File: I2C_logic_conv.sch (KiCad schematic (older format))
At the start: 5 parts

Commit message: アートワーク開始
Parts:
- Q1: renamed from Q?; footprint (none) -> SMD_Packages:SOT363
- R24, R25, R26, R27: renamed from R?; footprint (none) -> Resistors_SMD:R_0603
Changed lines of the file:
@@
 $Descr A4 11693 8268
 encoding utf-8
-Sheet 3 4
+Sheet 2 5
 Title ""
 Date ""
@@
 $EndDescr
 $Comp
-L BSS138PS Q?
+L BSS138PS Q1
 U 1 1 5838B8C7
 P 5850 3450
-AR Path="/583898DE/5838B8C7" Ref="Q?"  Part="1"
-AR Path="/58389DA7/5838B8C7" Ref="Q?"  Part="1"
-F 0 "Q?" H 6050 3900 50  0000 L CNN
+AR Path="/58389DA7/5838B8C7" Ref="Q1"  Part="1"
+AR Path="/583898DE/5838B8C7" Ref="Q2"  Part="1"
+AR Path="/583E5F3D/5838B8C7" Ref="Q3"  Part="1"
+F 0 "Q3" H 6050 3900 50  0000 L CNN
 F 1 "BSS138PS" H 5600 3900 50  0000 L CNN
-F 2 "" V 5775 3850 50  0001 L CIN
+F 2 "SMD_Packages:SOT363" V 5775 3850 50  0001 L CIN
 F 3 "" V 5850 3650 50  0000 L CNN
 	1    5850 3450
@@
 	5600 3550 4850 3550
 $Comp
-L R R?
+L R R24
 U 1 1 5838B993
 P 5050 2950
-AR Path="/583898DE/5838B993" Ref="R?"  Part="1"
-AR Path="/58389DA7/5838B993" Ref="R?"  Part="1"
-F 0 "R?" V 5130 2950 50  0000 C CNN
+AR Path="/58389DA7/5838B993" Ref="R24"  Part="1"
+AR Path="/583898DE/5838B993" Ref="R28"  Part="1"
+AR Path="/583E5F3D/5838B993" Ref="R33"  Part="1"
+F 0 "R33" V 5130 2950 50  0000 C CNN
 F 1 "R" V 5050 2950 50  0000 C CNN
-F 2 "" V 4980 2950 50  0000 C CNN
+F 2 "Resistors_SMD:R_0603" V 4980 2950 50  0001 C CNN
 F 3 "" H 5050 2950 50  0000 C CNN
 	1    5050 2950
@@
 $EndComp
 $Comp
-L R R?
+L R R25
 U 1 1 5838BA42
 P 5250 2950
-AR Path="/583898DE/5838BA42" Ref="R?"  Part="1"
-AR Path="/58389DA7/5838BA42" Ref="R?"  Part="1"
-F 0 "R?" V 5330 2950 50  0000 C CNN
+AR Path="/58389DA7/5838BA42" Ref="R25"  Part="1"
+AR Path="/583898DE/5838BA42" Ref="R29"  Part="1"
+AR Path="/583E5F3D/5838BA42" Ref="R34"  Part="1"
+F 0 "R34" V 5330 2950 50  0000 C CNN
 F 1 "R" V 5250 2950 50  0000 C CNN
-F 2 "" V 5180 2950 50  0000 C CNN
+F 2 "Resistors_SMD:R_0603" V 5180 2950 50  0001 C CNN
 F 3 "" H 5250 2950 50  0000 C CNN
 	1    5250 2950
@@
 Connection ~ 5250 3550
 $Comp
-L R R?
+L R R26
 U 1 1 5838BBE6
 P 6300 2900
-AR Path="/583898DE/5838BBE6" Ref="R?"  Part="1"
-AR Path="/58389DA7/5838BBE6" Ref="R?"  Part="1"
-F 0 "R?" V 6380 2900 50  0000 C CNN
+AR Path="/58389DA7/5838BBE6" Ref="R26"  Part="1"
+AR Path="/583898DE/5838BBE6" Ref="R30"  Part="1"
+AR Path="/583E5F3D/5838BBE6" Ref="R35"  Part="1"
+F 0 "R35" V 6380 2900 50  0000 C CNN
 F 1 "R" V 6300 2900 50  0000 C CNN
-F 2 "" V 6230 2900 50  0000 C CNN
+F 2 "Resistors_SMD:R_0603" V 6230 2900 50  0001 C CNN
 F 3 "" H 6300 2900 50  0000 C CNN
 	1    6300 2900
@@
 $EndComp
 $Comp
-L R R?
+L R R27
 U 1 1 5838BC03
 P 6500 2900
-AR Path="/583898DE/5838BC03" Ref="R?"  Part="1"
-AR Path="/58389DA7/5838BC03" Ref="R?"  Part="1"
-F 0 "R?" V 6580 2900 50  0000 C CNN
+AR Path="/58389DA7/5838BC03" Ref="R27"  Part="1"
+AR Path="/583898DE/5838BC03" Ref="R31"  Part="1"
+AR Path="/583E5F3D/5838BC03" Ref="R36"  Part="1"
+F 0 "R36" V 6580 2900 50  0000 C CNN
 F 1 "R" V 6500 2900 50  0000 C CNN
-F 2 "" V 6430 2900 50  0000 C CNN
+F 2 "Resistors_SMD:R_0603" V 6430 2900 50  0001 C CNN
 F 3 "" H 6500 2900 50  0000 C CNN
 	1    6500 2900

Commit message: 進捗
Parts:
- removed Q1: BSS138PS, SMD_Packages:SOT363, symbol BSS138PS
- added C6, C7: C, Capacitors_SMD:C_0603, symbol C
- added R14: R, Resistors_SMD:R_0603, symbol R
- added U4: PCA9306, Housings_SSOP:MSOP-8_3x3mm_Pitch0.65mm, symbol PCA9306
- renumbered R24 to R12, R25 to R13, R26 to R15, R27 to R16
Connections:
- net HV1: now also U4.6 (SCL2)
- net HV2: now also U4.5 (SDA2)
- net LV1: now also U4.3 (SCL1)
- net LV2: now also U4.4 (SDA1)
- net VH: now also R14.1
- net VL: now also C6.2, U4.2 (VREF1)
- new net: C7.2, R14.2, U4.7 (VREF2), U4.8 (EN)
- new net GND: C6.1, C7.1, U4.1 (GND)
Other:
- moved on the sheet: R23, R24, R26, R27

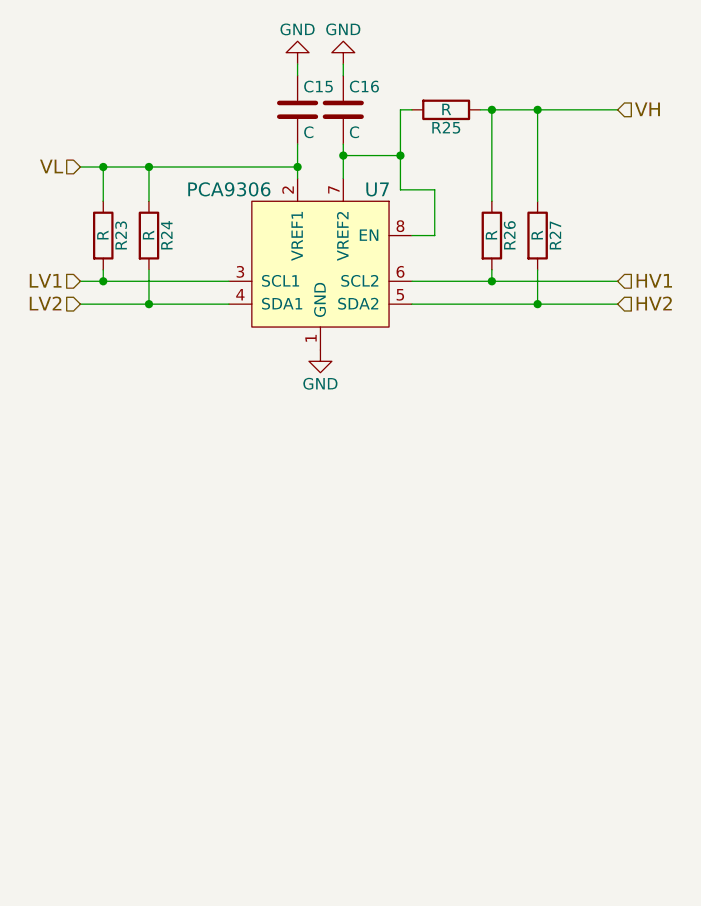
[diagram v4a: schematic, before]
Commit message: 図面にタイトルを追加
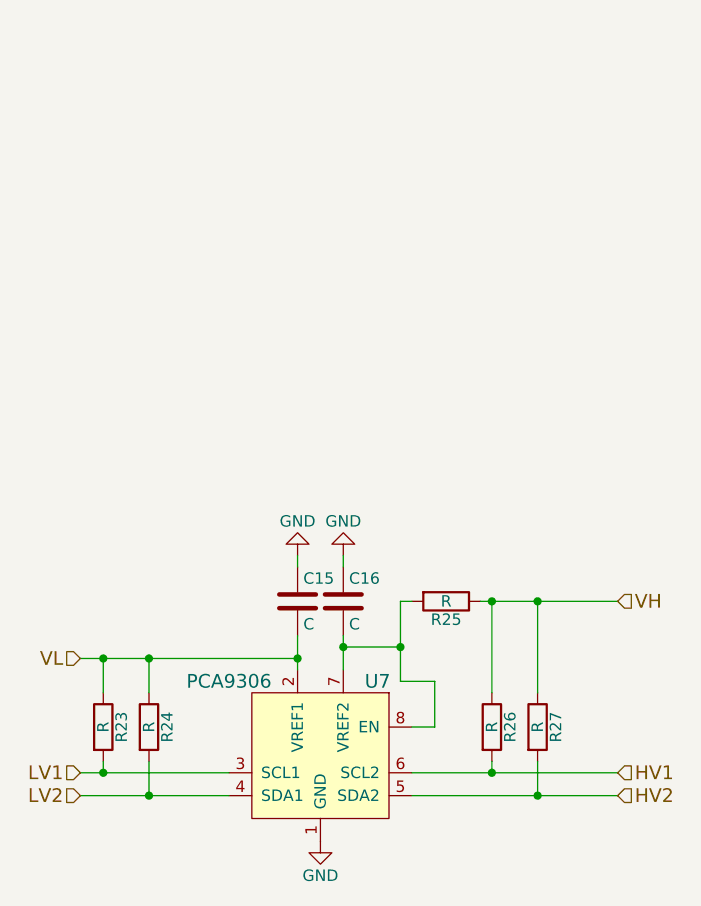
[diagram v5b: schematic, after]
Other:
- moved on the sheet: C15, C16, R23, R24, R25, R26, R27, U7
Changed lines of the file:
@@
 encoding utf-8
 Sheet 5 5
-Title ""
-Date ""
-Rev ""
-Comp ""
-Comment1 ""
-Comment2 ""
+Title "JetsonTK1_GPIO_Connector"
+Date "2016-12-18"
+Rev "1.1"
+Comp "Manju-Honpo"
+Comment1 "@C91"
+Comment2 "Designed by @yuqlid"
 Comment3 ""
 Comment4 ""
 $EndDescr
 Wire Wire Line
-	6300 2200 7200 2200
-Wire Wire Line
-	6300 2300 7200 2300
-Wire Wire Line
-	4850 2200 5500 2200
-Wire Wire Line
-	4850 2300 5500 2300
+	6300 4350 7200 4350
+Wire Wire Line
+	6300 4450 7200 4450
+Wire Wire Line
+	4850 4350 5500 4350
+Wire Wire Line
+	4850 4450 5500 4450
 $Comp
 L R R12
 U 1 1 5838B993
-P 4950 2000
+P 4950 4150
 AR Path="/58389DA7/5838B993" Ref="R12"  Part="1"
 AR Path="/583898DE/5838B993" Ref="R17"  Part="1"
 AR Path="/583E5F3D/5838B993" Ref="R23"  Part="1"
-F 0 "R23" V 5030 2000 50  0000 C CNN
-F 1 "R" V 4950 2000 50  0000 C CNN
-F 2 "Resistors_SMD:R_0603" V 4880 2000 50  0001 C CNN
-F 3 "" H 4950 2000 50  0000 C CNN
-	1    4950 2000
+F 0 "R23" V 5030 4150 50  0000 C CNN
+F 1 "R" V 4950 4150 50  0000 C CNN
+F 2 "Resistors_SMD:R_0603" V 4880 4150 50  0001 C CNN
+F 3 "" H 4950 4150 50  0000 C CNN
+	1    4950 4150
 	1    0    0    -1
 $EndComp
@@
 L R R13
 U 1 1 5838BA42
-P 5150 2000
+P 5150 4150
 AR Path="/58389DA7/5838BA42" Ref="R13"  Part="1"
 AR Path="/583898DE/5838BA42" Ref="R18"  Part="1"
 AR Path="/583E5F3D/5838BA42" Ref="R24"  Part="1"
-F 0 "R24" V 5230 2000 50  0000 C CNN
-F 1 "R" V 5150 2000 50  0000 C CNN
-F 2 "Resistors_SMD:R_0603" V 5080 2000 50  0001 C CNN
-F 3 "" H 5150 2000 50  0000 C CNN
-	1    5150 2000
-	1    0    0    -1
-$EndComp
-Wire Wire Line
-	4850 1700 5800 1700
-Wire Wire Line
-	5150 1850 5150 1700
-Connection ~ 5150 1700
-Wire Wire Line
-	4950 1850 4950 1700
-Connection ~ 4950 1700
-Wire Wire Line
-	4950 2150 4950 2200
-Connection ~ 4950 2200
-Wire Wire Line
-	5150 2150 5150 2300
-Connection ~ 5150 2300
+F 0 "R24" V 5230 4150 50  0000 C CNN
+F 1 "R" V 5150 4150 50  0000 C CNN
+F 2 "Resistors_SMD:R_0603" V 5080 4150 50  0001 C CNN
+F 3 "" H 5150 4150 50  0000 C CNN
+	1    5150 4150
+	1    0    0    -1
+$EndComp
+Wire Wire Line
+	4850 3850 5800 3850
+Wire Wire Line
+	5150 4000 5150 3850
+Connection ~ 5150 3850
+Wire Wire Line
+	4950 4000 4950 3850
+Connection ~ 4950 3850
+Wire Wire Line
+	4950 4300 4950 4350
+Connection ~ 4950 4350
+Wire Wire Line
+	5150 4300 5150 4450
+Connection ~ 5150 4450
 $Comp
 L R R15
 U 1 1 5838BBE6
-P 6650 2000
+P 6650 4150
 AR Path="/58389DA7/5838BBE6" Ref="R15"  Part="1"
 AR Path="/583898DE/5838BBE6" Ref="R20"  Part="1"
 AR Path="/583E5F3D/5838BBE6" Ref="R26"  Part="1"
-F 0 "R26" V 6730 2000 50  0000 C CNN
-F 1 "R" V 6650 2000 50  0000 C CNN
-F 2 "Resistors_SMD:R_0603" V 6580 2000 50  0001 C CNN
-F 3 "" H 6650 2000 50  0000 C CNN
-	1    6650 2000
+F 0 "R26" V 6730 4150 50  0000 C CNN
+F 1 "R" V 6650 4150 50  0000 C CNN
+F 2 "Resistors_SMD:R_0603" V 6580 4150 50  0001 C CNN
+F 3 "" H 6650 4150 50  0000 C CNN
+	1    6650 4150
 	1    0    0    -1
 $EndComp
@@
 L R R16
 U 1 1 5838BC03
-P 6850 2000
+P 6850 4150
 AR Path="/58389DA7/5838BC03" Ref="R16"  Part="1"
 AR Path="/583898DE/5838BC03" Ref="R21"  Part="1"
 AR Path="/583E5F3D/5838BC03" Ref="R27"  Part="1"
-F 0 "R27" V 6930 2000 50  0000 C CNN
-F 1 "R" V 6850 2000 50  0000 C CNN
-F 2 "Resistors_SMD:R_0603" V 6780 2000 50  0001 C CNN
-F 3 "" H 6850 2000 50  0000 C CNN
-	1    6850 2000
-	1    0    0    -1
-$EndComp
-Wire Wire Line
-	6650 1850 6650 1450
-Wire Wire Line
-	6600 1450 7200 1450
-Wire Wire Line
-	6850 1850 6850 1450
-Connection ~ 6850 1450
-Wire Wire Line
-	6650 2150 6650 2200
-Connection ~ 6650 2200
-Wire Wire Line
-	6850 2150 6850 2300
-Connection ~ 6850 2300
-Text HLabel 4850 1700 0    60   Input ~ 0
+F 0 "R27" V 6930 4150 50  0000 C CNN
+F 1 "R" V 6850 4150 50  0000 C CNN
+F 2 "Resistors_SMD:R_0603" V 6780 4150 50  0001 C CNN
+F 3 "" H 6850 4150 50  0000 C CNN
+	1    6850 4150
+	1    0    0    -1
+$EndComp
+Wire Wire Line
+	6650 4000 6650 3600
+Wire Wire Line
+	6600 3600 7200 3600
+Wire Wire Line
+	6850 4000 6850 3600
+Connection ~ 6850 3600
+Wire Wire Line
+	6650 4300 6650 4350
+Connection ~ 6650 4350
+Wire Wire Line
+	6850 4300 6850 4450
+Connection ~ 6850 4450
+Text HLabel 4850 3850 0    60   Input ~ 0
 VL
-Text HLabel 7200 1450 2    60   Input ~ 0
+Text HLabel 7200 3600 2    60   Input ~ 0
 VH
-Text HLabel 4850 2200 0    60   Input ~ 0
+Text HLabel 4850 4350 0    60   Input ~ 0
 LV1
-Text HLabel 4850 2300 0    60   Input ~ 0
+Text HLabel 4850 4450 0    60   Input ~ 0
 LV2
-Text HLabel 7200 2200 2    60   Input ~ 0
+Text HLabel 7200 4350 2    60   Input ~ 0
 HV1
-Text HLabel 7200 2300 2    60   Input ~ 0
+Text HLabel 7200 4450 2    60   Input ~ 0
 HV2
 $Comp
 L PCA9306 U4
 U 1 1 583C3211
-P 5900 2200
+P 5900 4350
 AR Path="/58389DA7/583C3211" Ref="U4"  Part="1"
 AR Path="/583898DE/583C3211" Ref="U5"  Part="1"
 AR Path="/583E5F3D/583C3211" Ref="U7"  Part="1"
-F 0 "U7" H 6150 2600 60  0000 C CNN
-F 1 "PCA9306" H 5500 2600 60  0000 C CNN
-F 2 "Housings_SSOP:MSOP-8_3x3mm_Pitch0.65mm" H 5800 2200 60  0001 C CNN
-F 3 "" H 5800 2200 60  0001 C CNN
-	1    5900 2200
-	1    0    0    -1
-$EndComp
-Wire Wire Line
-	5800 1600 5800 1750
+F 0 "U7" H 6150 4750 60  0000 C CNN
+F 1 "PCA9306" H 5500 4750 60  0000 C CNN
+F 2 "Housings_SSOP:MSOP-8_3x3mm_Pitch0.65mm" H 5800 4350 60  0001 C CNN
+F 3 "" H 5800 4350 60  0001 C CNN
+	1    5900 4350
+	1    0    0    -1
+$EndComp
+Wire Wire Line
+	5800 3750 5800 3900
 $Comp
 L GND #PWR087
 U 1 1 583C3B42
-P 5900 2500
+P 5900 4650
 AR Path="/58389DA7/583C3B42" Ref="#PWR087"  Part="1"
 AR Path="/583898DE/583C3B42" Ref="#PWR090"  Part="1"
 AR Path="/583E5F3D/583C3B42" Ref="#PWR0101"  Part="1"
-F 0 "#PWR0101" H 5900 2250 50  0001 C CNN
-F 1 "GND" H 5900 2350 50  0000 C CNN
-F 2 "" H 5900 2500 50  0000 C CNN
-F 3 "" H 5900 2500 50  0000 C CNN
-	1    5900 2500
+F 0 "#PWR0101" H 5900 4400 50  0001 C CNN
+F 1 "GND" H 5900 4500 50  0000 C CNN
+F 2 "" H 5900 4650 50  0000 C CNN
+F 3 "" H 5900 4650 50  0000 C CNN
+	1    5900 4650
 	1    0    0    -1
 $EndComp
@@
 L C C6
 U 1 1 583C3E21
-P 5800 1450
+P 5800 3600
 AR Path="/58389DA7/583C3E21" Ref="C6"  Part="1"
 AR Path="/583898DE/583C3E21" Ref="C8"  Part="1"
 AR Path="/583E5F3D/583C3E21" Ref="C15"  Part="1"
-F 0 "C15" H 5825 1550 50  0000 L CNN
-F 1 "C" H 5825 1350 50  0000 L CNN
-F 2 "Capacitors_SMD:C_0603" H 5838 1300 50  0001 C CNN
-F 3 "" H 5800 1450 50  0000 C CNN
-	1    5800 1450
+F 0 "C15" H 5825 3700 50  0000 L CNN
+F 1 "C" H 5825 3500 50  0000 L CNN
+F 2 "Capacitors_SMD:C_0603" H 5838 3450 50  0001 C CNN
+F 3 "" H 5800 3600 50  0000 C CNN
+	1    5800 3600
 	1    0    0    -1
 $EndComp
@@
 L C C7
 U 1 1 583C3EB8
-P 6000 1450
+P 6000 3600
 AR Path="/58389DA7/583C3EB8" Ref="C7"  Part="1"
 AR Path="/583898DE/583C3EB8" Ref="C9"  Part="1"
 AR Path="/583E5F3D/583C3EB8" Ref="C16"  Part="1"
-F 0 "C16" H 6025 1550 50  0000 L CNN
-F 1 "C" H 6025 1350 50  0000 L CNN
-F 2 "Capacitors_SMD:C_0603" H 6038 1300 50  0001 C CNN
-F 3 "" H 6000 1450 50  0000 C CNN
-	1    6000 1450
+F 0 "C16" H 6025 3700 50  0000 L CNN
+F 1 "C" H 6025 3500 50  0000 L CNN
+F 2 "Capacitors_SMD:C_0603" H 6038 3450 50  0001 C CNN
+F 3 "" H 6000 3600 50  0000 C CNN
+	1    6000 3600
 	1    0    0    -1
 $EndComp
@@
 L GND #PWR088
 U 1 1 583C3F2C
-P 5800 1250
+P 5800 3400
 AR Path="/58389DA7/583C3F2C" Ref="#PWR088"  Part="1"
 AR Path="/583898DE/583C3F2C" Ref="#PWR091"  Part="1"
 AR Path="/583E5F3D/583C3F2C" Ref="#PWR0102"  Part="1"
-F 0 "#PWR0102" H 5800 1000 50  0001 C CNN
-F 1 "GND" H 5800 1100 50  0000 C CNN
-F 2 "" H 5800 1250 50  0000 C CNN
-F 3 "" H 5800 1250 50  0000 C CNN
-	1    5800 1250
+F 0 "#PWR0102" H 5800 3150 50  0001 C CNN
+F 1 "GND" H 5800 3250 50  0000 C CNN
+F 2 "" H 5800 3400 50  0000 C CNN
+F 3 "" H 5800 3400 50  0000 C CNN
+	1    5800 3400
 	-1   0    0    1
 $EndComp
 Wire Wire Line
-	5800 1250 5800 1300
-Connection ~ 5800 1700
-Wire Wire Line
-	6000 1600 6000 1750
+	5800 3400 5800 3450
+Connection ~ 5800 3850
+Wire Wire Line
+	6000 3750 6000 3900
 $Comp
 L GND #PWR089
 U 1 1 583C4151
-P 6000 1250
+P 6000 3400
 AR Path="/58389DA7/583C4151" Ref="#PWR089"  Part="1"
 AR Path="/583898DE/583C4151" Ref="#PWR092"  Part="1"
 AR Path="/583E5F3D/583C4151" Ref="#PWR0103"  Part="1"
-F 0 "#PWR0103" H 6000 1000 50  0001 C CNN
-F 1 "GND" H 6000 1100 50  0000 C CNN
-F 2 "" H 6000 1250 50  0000 C CNN
-F 3 "" H 6000 1250 50  0000 C CNN
-	1    6000 1250
+F 0 "#PWR0103" H 6000 3150 50  0001 C CNN
+F 1 "GND" H 6000 3250 50  0000 C CNN
+F 2 "" H 6000 3400 50  0000 C CNN
+F 3 "" H 6000 3400 50  0000 C CNN
+	1    6000 3400
 	-1   0    0    1
 $EndComp
 Wire Wire Line
-	6000 1250 6000 1300
+	6000 3400 6000 3450
 $Comp
 L R R14
 U 1 1 583C426E
-P 6450 1450
+P 6450 3600
 AR Path="/58389DA7/583C426E" Ref="R14"  Part="1"
 AR Path="/583898DE/583C426E" Ref="R19"  Part="1"
 AR Path="/583E5F3D/583C426E" Ref="R25"  Part="1"
-F 0 "R25" V 6530 1450 50  0000 C CNN
-F 1 "R" V 6450 1450 50  0000 C CNN
-F 2 "Resistors_SMD:R_0603" V 6380 1450 50  0001 C CNN
-F 3 "" H 6450 1450 50  0000 C CNN
-	1    6450 1450
+F 0 "R25" V 6530 3600 50  0000 C CNN
+F 1 "R" V 6450 3600 50  0000 C CNN
+F 2 "Resistors_SMD:R_0603" V 6380 3600 50  0001 C CNN
+F 3 "" H 6450 3600 50  0000 C CNN
+	1    6450 3600
 	0    1    1    0
 $EndComp
-Connection ~ 6650 1450
-Wire Wire Line
-	6300 1450 6250 1450
-Wire Wire Line
-	6250 1450 6250 1800
-Wire Wire Line
-	6250 1800 6400 1800
-Wire Wire Line
-	6400 1800 6400 2000
-Wire Wire Line
-	6400 2000 6300 2000
-Wire Wire Line
-	6000 1650 6250 1650
-Connection ~ 6250 1650
-Connection ~ 6000 1650
+Connection ~ 6650 3600
+Wire Wire Line
+	6300 3600 6250 3600
+Wire Wire Line
+	6250 3600 6250 3950
+Wire Wire Line
+	6250 3950 6400 3950
+Wire Wire Line
+	6400 3950 6400 4150
+Wire Wire Line
+	6400 4150 6300 4150
+Wire Wire Line
+	6000 3800 6250 3800
+Connection ~ 6250 3800
+Connection ~ 6000 3800
 $EndSCHEMATC

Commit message: 名称変更，再アノテーション
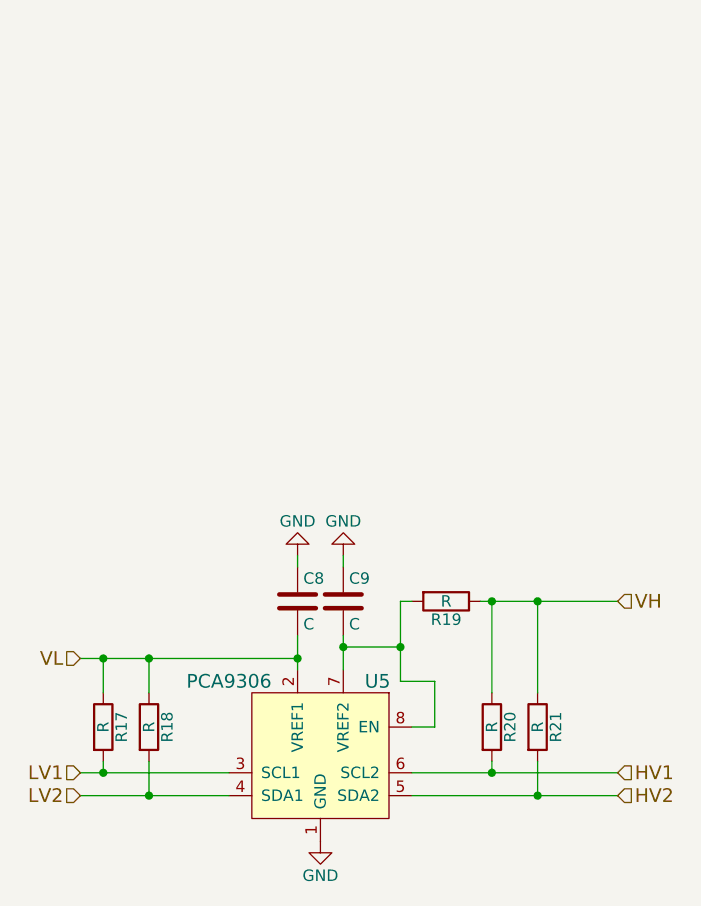
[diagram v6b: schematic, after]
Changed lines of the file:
@@
 encoding utf-8
 Sheet 5 5
-Title "JetsonTK1_GPIO_Connector"
+Title "JetsonTK1_Expand_Board"
 Date "2016-12-18"
 Rev "1.1"
@@
 AR Path="/583898DE/5838B993" Ref="R17"  Part="1"
 AR Path="/583E5F3D/5838B993" Ref="R23"  Part="1"
-F 0 "R23" V 5030 4150 50  0000 C CNN
+F 0 "R17" V 5030 4150 50  0000 C CNN
 F 1 "R" V 4950 4150 50  0000 C CNN
 F 2 "Resistors_SMD:R_0603" V 4880 4150 50  0001 C CNN
@@
 AR Path="/583898DE/5838BA42" Ref="R18"  Part="1"
 AR Path="/583E5F3D/5838BA42" Ref="R24"  Part="1"
-F 0 "R24" V 5230 4150 50  0000 C CNN
+F 0 "R18" V 5230 4150 50  0000 C CNN
 F 1 "R" V 5150 4150 50  0000 C CNN
 F 2 "Resistors_SMD:R_0603" V 5080 4150 50  0001 C CNN
@@
 AR Path="/583898DE/5838BBE6" Ref="R20"  Part="1"
 AR Path="/583E5F3D/5838BBE6" Ref="R26"  Part="1"
-F 0 "R26" V 6730 4150 50  0000 C CNN
+F 0 "R20" V 6730 4150 50  0000 C CNN
 F 1 "R" V 6650 4150 50  0000 C CNN
 F 2 "Resistors_SMD:R_0603" V 6580 4150 50  0001 C CNN
@@
 AR Path="/583898DE/5838BC03" Ref="R21"  Part="1"
 AR Path="/583E5F3D/5838BC03" Ref="R27"  Part="1"
-F 0 "R27" V 6930 4150 50  0000 C CNN
+F 0 "R21" V 6930 4150 50  0000 C CNN
 F 1 "R" V 6850 4150 50  0000 C CNN
 F 2 "Resistors_SMD:R_0603" V 6780 4150 50  0001 C CNN
@@
 AR Path="/583898DE/583C3211" Ref="U5"  Part="1"
 AR Path="/583E5F3D/583C3211" Ref="U7"  Part="1"
-F 0 "U7" H 6150 4750 60  0000 C CNN
+F 0 "U5" H 6150 4750 60  0000 C CNN
 F 1 "PCA9306" H 5500 4750 60  0000 C CNN
 F 2 "Housings_SSOP:MSOP-8_3x3mm_Pitch0.65mm" H 5800 4350 60  0001 C CNN
@@
 AR Path="/583898DE/583C3B42" Ref="#PWR090"  Part="1"
 AR Path="/583E5F3D/583C3B42" Ref="#PWR0101"  Part="1"
-F 0 "#PWR0101" H 5900 4400 50  0001 C CNN
+F 0 "#PWR090" H 5900 4400 50  0001 C CNN
 F 1 "GND" H 5900 4500 50  0000 C CNN
 F 2 "" H 5900 4650 50  0000 C CNN
@@
 AR Path="/583898DE/583C3E21" Ref="C8"  Part="1"
 AR Path="/583E5F3D/583C3E21" Ref="C15"  Part="1"
-F 0 "C15" H 5825 3700 50  0000 L CNN
+F 0 "C8" H 5825 3700 50  0000 L CNN
 F 1 "C" H 5825 3500 50  0000 L CNN
 F 2 "Capacitors_SMD:C_0603" H 5838 3450 50  0001 C CNN
@@
 AR Path="/583898DE/583C3EB8" Ref="C9"  Part="1"
 AR Path="/583E5F3D/583C3EB8" Ref="C16"  Part="1"
-F 0 "C16" H 6025 3700 50  0000 L CNN
+F 0 "C9" H 6025 3700 50  0000 L CNN
 F 1 "C" H 6025 3500 50  0000 L CNN
 F 2 "Capacitors_SMD:C_0603" H 6038 3450 50  0001 C CNN
@@
 AR Path="/583898DE/583C3F2C" Ref="#PWR091"  Part="1"
 AR Path="/583E5F3D/583C3F2C" Ref="#PWR0102"  Part="1"
-F 0 "#PWR0102" H 5800 3150 50  0001 C CNN
+F 0 "#PWR091" H 5800 3150 50  0001 C CNN
 F 1 "GND" H 5800 3250 50  0000 C CNN
 F 2 "" H 5800 3400 50  0000 C CNN
@@
 AR Path="/583898DE/583C4151" Ref="#PWR092"  Part="1"
 AR Path="/583E5F3D/583C4151" Ref="#PWR0103"  Part="1"
-F 0 "#PWR0103" H 6000 3150 50  0001 C CNN
+F 0 "#PWR092" H 6000 3150 50  0001 C CNN
 F 1 "GND" H 6000 3250 50  0000 C CNN
 F 2 "" H 6000 3400 50  0000 C CNN
@@
 AR Path="/583898DE/583C426E" Ref="R19"  Part="1"
 AR Path="/583E5F3D/583C426E" Ref="R25"  Part="1"
-F 0 "R25" V 6530 3600 50  0000 C CNN
+F 0 "R19" V 6530 3600 50  0000 C CNN
 F 1 "R" V 6450 3600 50  0000 C CNN
 F 2 "Resistors_SMD:R_0603" V 6380 3600 50  0001 C CNN
